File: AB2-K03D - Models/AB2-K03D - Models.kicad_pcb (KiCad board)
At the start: 2 copper layers, 129 parts

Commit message: AB2-K03D: add RJ45 connector
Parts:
- added AB2_RJ45_RA_LEDS: VAL**, AB2_RJ45_RA_LEDS, F.Cu at (158.5, 276.6)

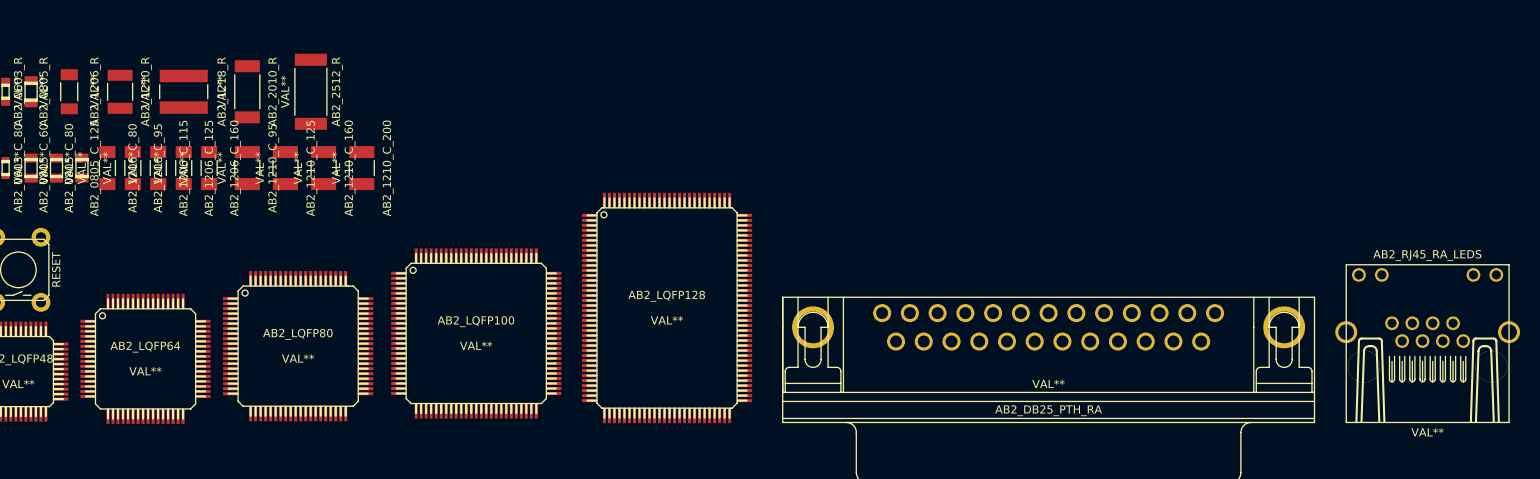
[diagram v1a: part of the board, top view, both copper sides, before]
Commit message: AB2-K03D: added soic packages
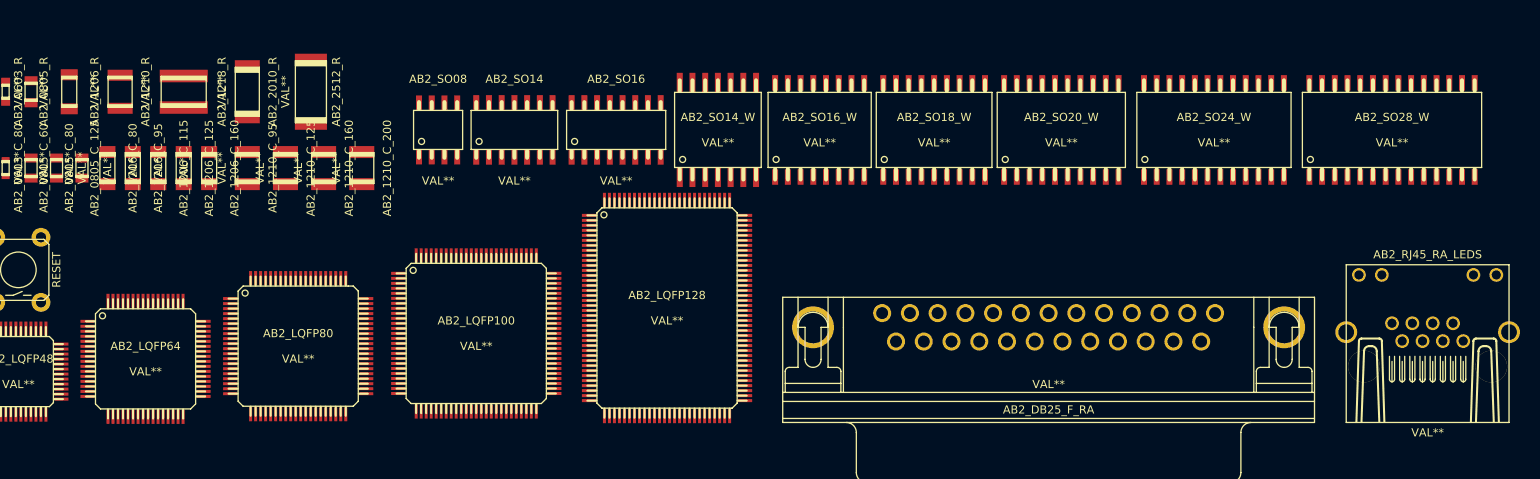
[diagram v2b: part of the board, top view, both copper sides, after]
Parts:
- removed AB2_DB25_PTH_RA: VAL**, AB2_DB25_PTH_RA
- added AB2_DB25_F_RA: VAL**, AB2_DB25_F_RA, F.Cu at (120.7, 284.5)
- added AB2_SO08: VAL**, AB2_SO08, F.Cu at (59.7, 255.3)
- added AB2_SO14: VAL**, AB2_SO14, F.Cu at (67.3, 255.3)
- added AB2_SO14_W: VAL**, AB2_SO14_W, F.Cu at (87.6, 255.3)
- added AB2_SO16: VAL**, AB2_SO16, F.Cu at (77.5, 255.3)
- added AB2_SO16_W: VAL**, AB2_SO16_W, F.Cu at (97.8, 255.3)
- added AB2_SO18_W: VAL**, AB2_SO18_W, F.Cu at (109.2, 255.3)
- added AB2_SO20_W: VAL**, AB2_SO20_W, F.Cu at (121.9, 255.3)
- added AB2_SO24_W: VAL**, AB2_SO24_W, F.Cu at (137.2, 255.3)
- added AB2_SO28_W: VAL**, AB2_SO28_W, F.Cu at (154.9, 255.3)
